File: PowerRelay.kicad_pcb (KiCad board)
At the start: 2 copper layers, 100 x 100 mm, 26 parts, among them J1 Screw_Terminal_01x03, J2 Conn_01x20_Female, J3 Conn_01x20_Female, J4 Conn_01x02_Female, J5 Screw_Terminal_01x03, J6 Screw_Terminal_01x03, J7 Conn_01x02_Female, K1 G5LE-1A4_DC3, K2 G5LE-1A4_DC3, Q1 2N7000, Q2 2N7000

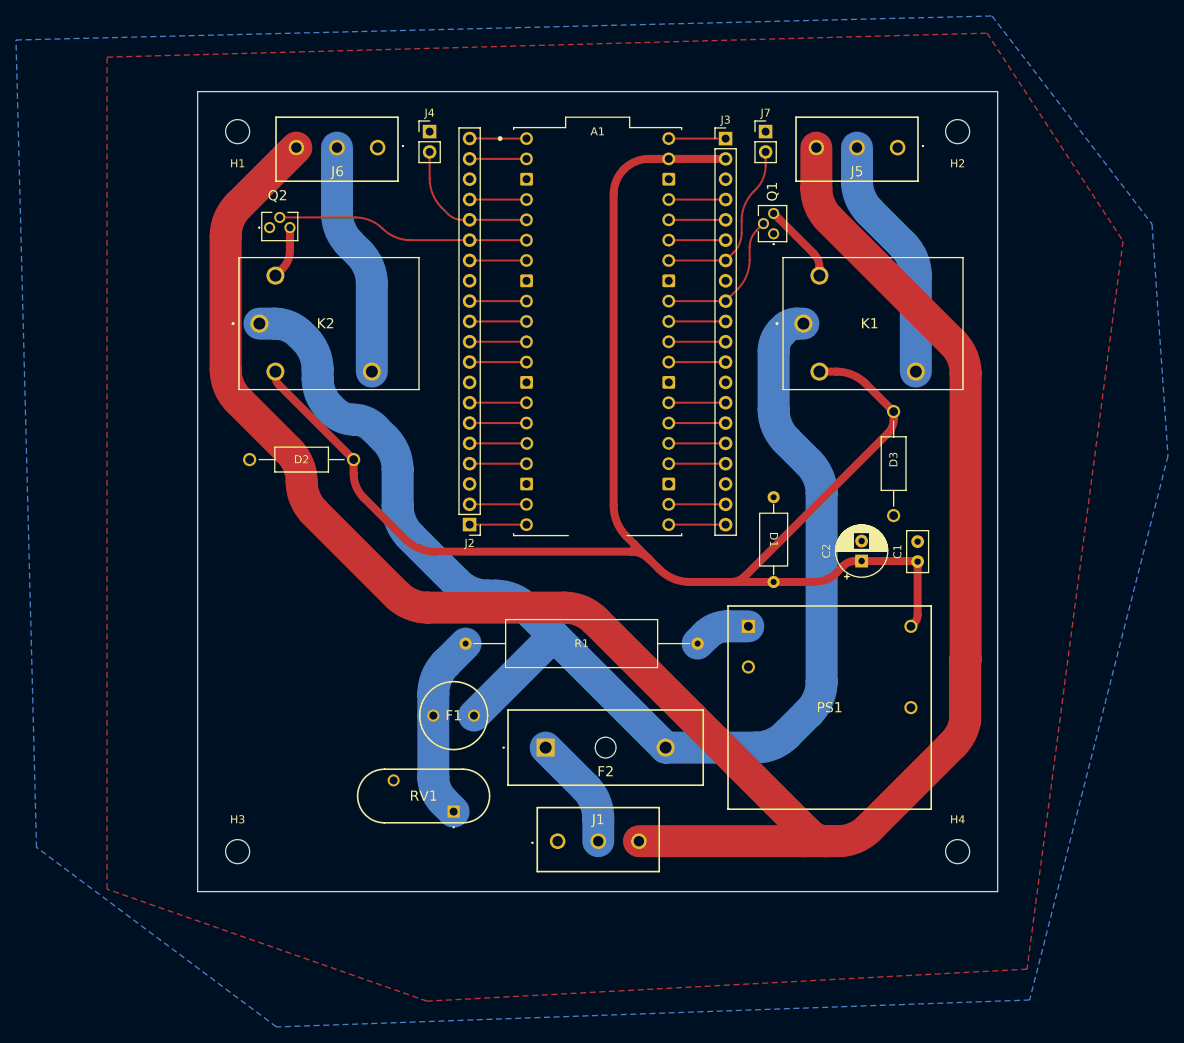
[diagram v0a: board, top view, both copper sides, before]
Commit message: add power label for ac power connectors to silkscreen
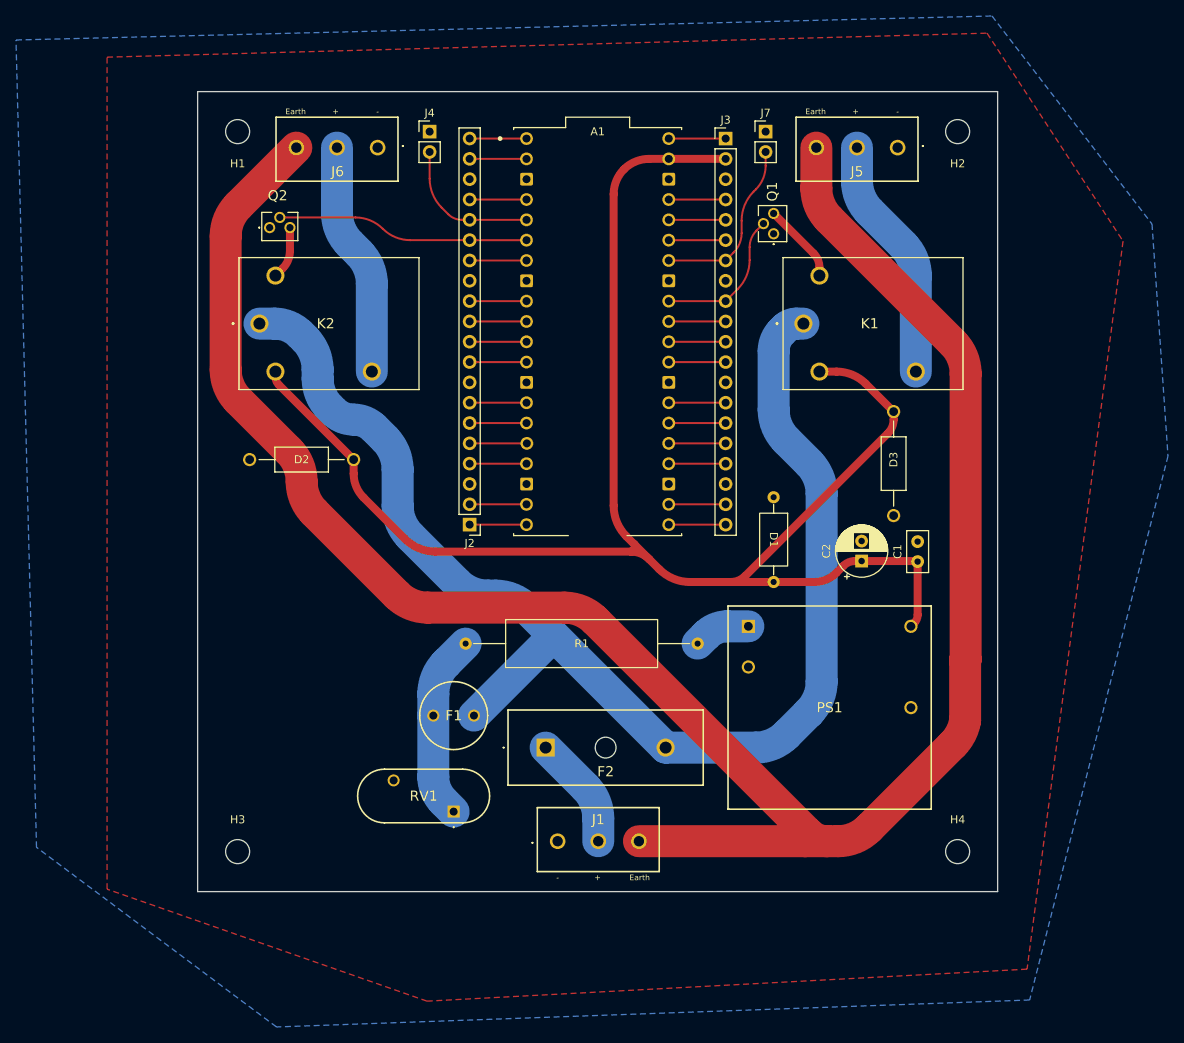
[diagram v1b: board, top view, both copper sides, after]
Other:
- board text added: "+"
- board text added: "-"
- board text added: "Earth"
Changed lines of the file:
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@@
   )
   (gr_rect (start 50 50) (end 150 150) (layer "Edge.Cuts") (width 0.1) (fill none))
+  (gr_text "-" (at 95 148.25) (layer "F.SilkS")
+    (effects (font (size 0.7 0.7) (thickness 0.15)))
+  )
+  (gr_text "+" (at 67.25 52.5) (layer "F.SilkS")
+    (effects (font (size 0.7 0.7) (thickness 0.15)))
+  )
+  (gr_text "-" (at 72.5 52.5) (layer "F.SilkS")
+    (effects (font (size 0.7 0.7) (thickness 0.15)))
+  )
+  (gr_text "Earth" (at 62.25 52.5) (layer "F.SilkS")
+    (effects (font (size 0.7 0.7) (thickness 0.15)))
+  )
+  (gr_text "Earth" (at 127.25 52.5) (layer "F.SilkS")
+    (effects (font (size 0.7 0.7) (thickness 0.15)))
+  )
+  (gr_text "-" (at 137.5 52.5) (layer "F.SilkS")
+    (effects (font (size 0.7 0.7) (thickness 0.15)))
+  )
+  (gr_text "Earth" (at 105.25 148.25) (layer "F.SilkS")
+    (effects (font (size 0.7 0.7) (thickness 0.15)))
+  )
+  (gr_text "+" (at 132.25 52.5) (layer "F.SilkS")
+    (effects (font (size 0.7 0.7) (thickness 0.15)))
+  )
+  (gr_text "+" (at 100 148.25) (layer "F.SilkS")
+    (effects (font (size 0.7 0.7) (thickness 0.15)))
+  )
   (segment (start 59.725 85.6125) (end 59.725 85) (width 1) (layer "F.Cu") (net 1))
   (segment (start 104.546896 106.546896) (end 106.453104 108.453104) (width 1) (layer "F.Cu") (net 1))

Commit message: added intruction for later
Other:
- board text added: "put wire connector here move pico back to accomidate"
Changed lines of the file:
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@@
     (pad "" np_thru_hole circle (at 0 0) (size 3 3) (drill 3) (layers *.Cu *.Mask))
   )
+  (gr_rect (start 96 52) (end 104 55) (layer "Dwgs.User") (width 0.15) (fill none))
   (gr_rect (start 50 50) (end 150 150) (layer "Edge.Cuts") (width 0.1) (fill none))
   (gr_text "-" (at 95 148.25) (layer "F.SilkS")
@@
     (effects (font (size 0.7 0.7) (thickness 0.15)))
   )
+  (gr_text "put wire connector here move pico back to accomidate" (at 100 53) (layer "Dwgs.User")
+    (effects (font (size 1 1) (thickness 0.15)))
+  )
   (segment (start 59.725 85.6125) (end 59.725 85) (width 1) (layer "F.Cu") (net 1))

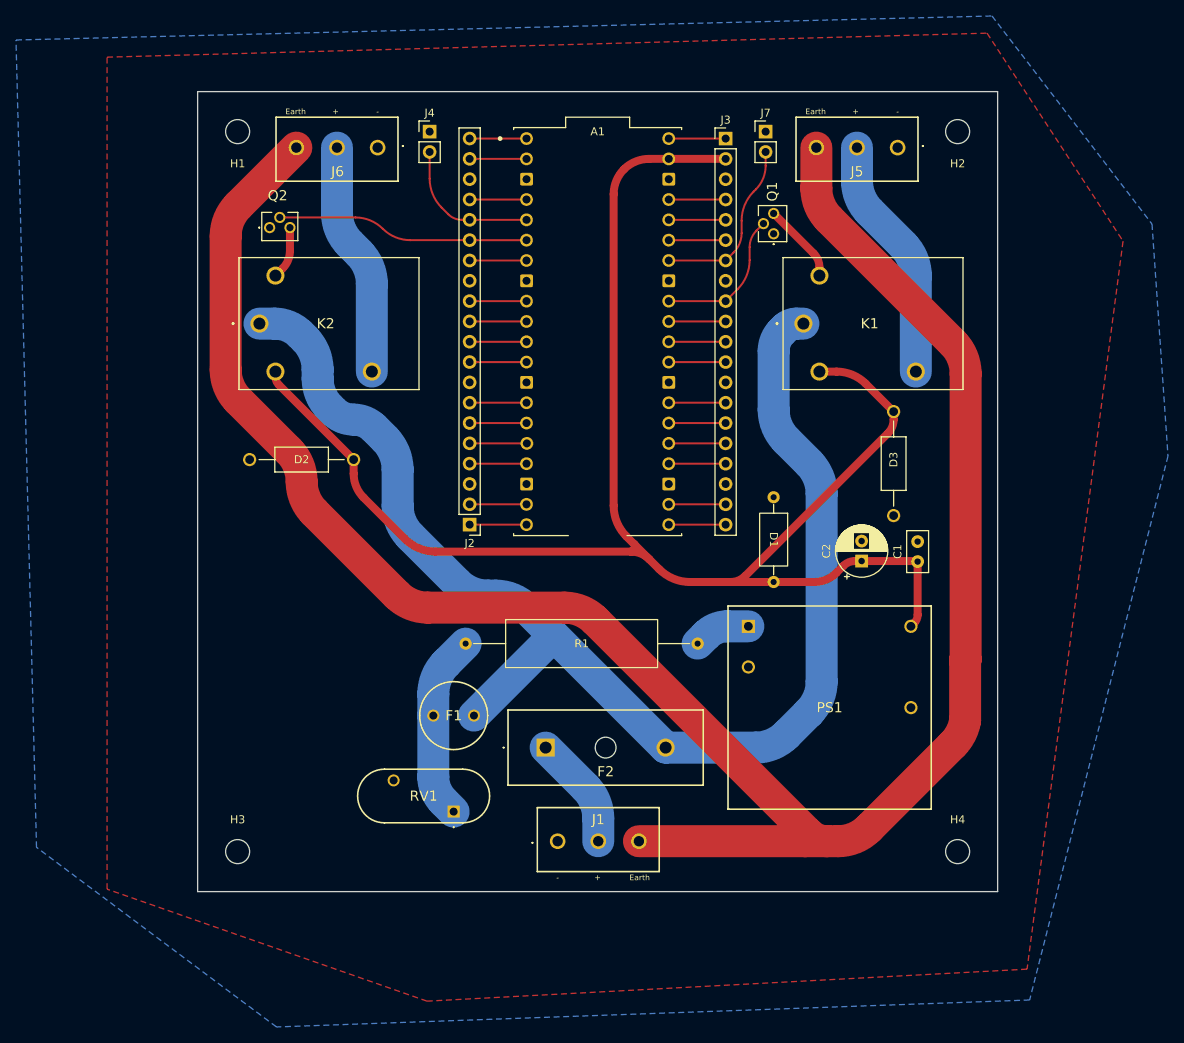
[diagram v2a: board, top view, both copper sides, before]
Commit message: add aux port for inter board comunication
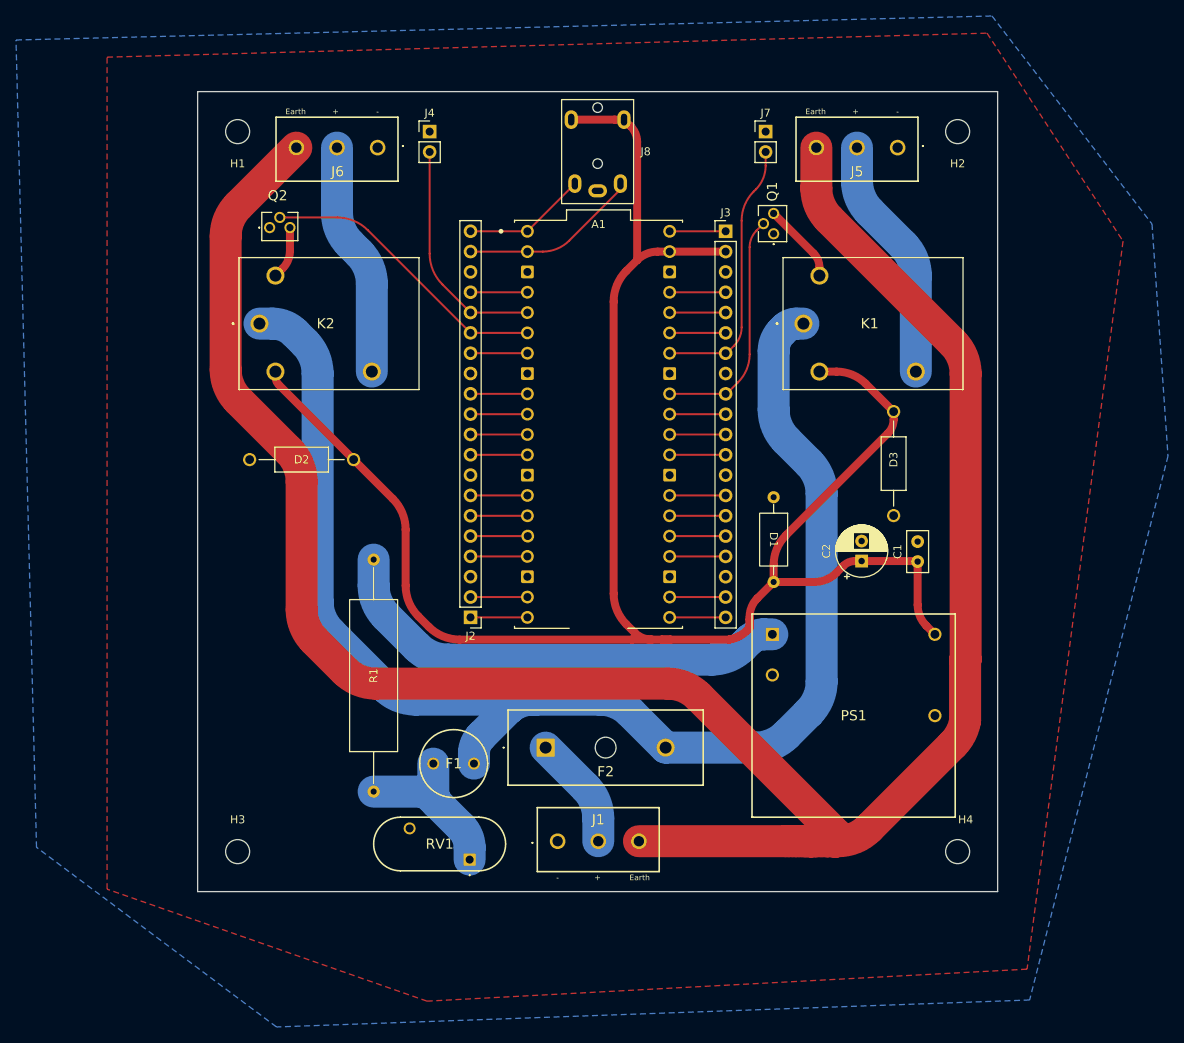
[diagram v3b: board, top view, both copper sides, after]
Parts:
- added J8: AudioJack4, 54-00174:54-00174_JACK, F.Cu at (103.5, 50.0)
- moved R1 26.3 mm to (72.0, 123.0), turned to 90 degrees
- moved A1 11.6 mm to (100.1, 91.6)
- moved J2 11.6 mm to (84.1, 115.7)
- moved J3 11.6 mm to (116.0, 67.5)
- moved RV1 6.32 mm to (84.0, 146.0)
- moved F1 6.00 mm to (84.5, 134.0)
- moved PS1 3.16 mm to (121.8, 117.8)
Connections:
- net Net-(A1-Pad1) renamed TX
- net Net-(A1-Pad2) renamed RX
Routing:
- net Net-(PS1-Pad1): track 7.06 -> 58.6 mm
- net +3V3: track 209.3 -> 246.1 mm
- net RX: track 7.11 -> 22.4 mm
- net Heating: track 18.4 -> 29.9 mm
- net VAC: track 166.3 -> 177.6 mm
- net Cooling Switch: track 18.5 -> 29.0 mm
- net Heating SW: track 23.0 -> 33.5 mm
- net Earth: track 260.7 -> 270.9 mm
- net TX: track 7.11 -> 15.5 mm
- net Cooling: track 31.5 -> 36.7 mm
- net Net-(F1-Pad2): track 23.3 -> 22.7 mm
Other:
- board text removed: "put wire connector here move pico back to accomidate"

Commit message: add logo to board
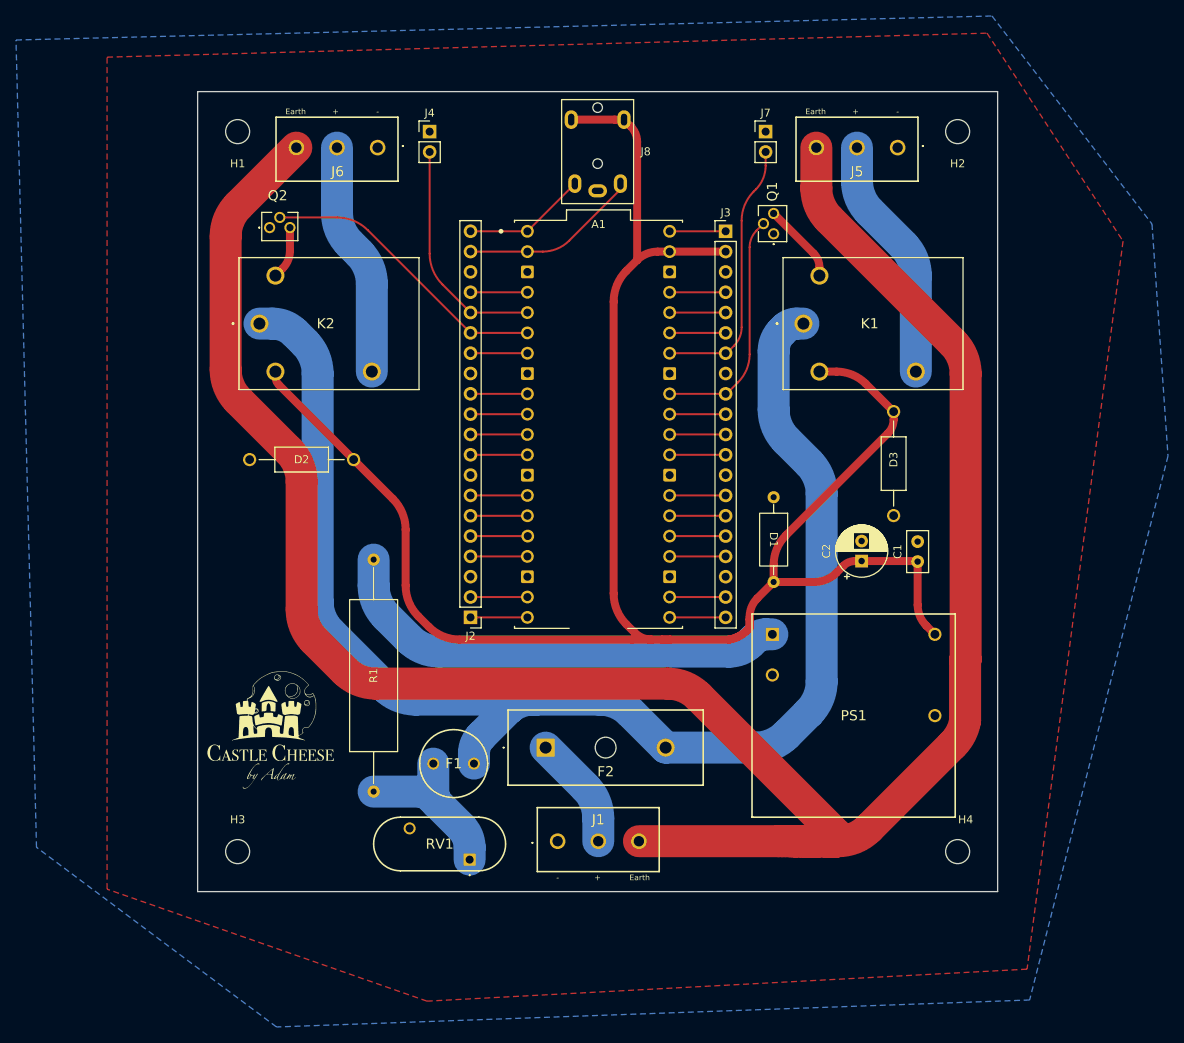
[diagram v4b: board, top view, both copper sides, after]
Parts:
- added G***: LOGO, PCB:Logo, F.Cu at (59.0, 130.0)
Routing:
- net Net-(PS1-Pad1): track 58.6 -> 57.9 mm

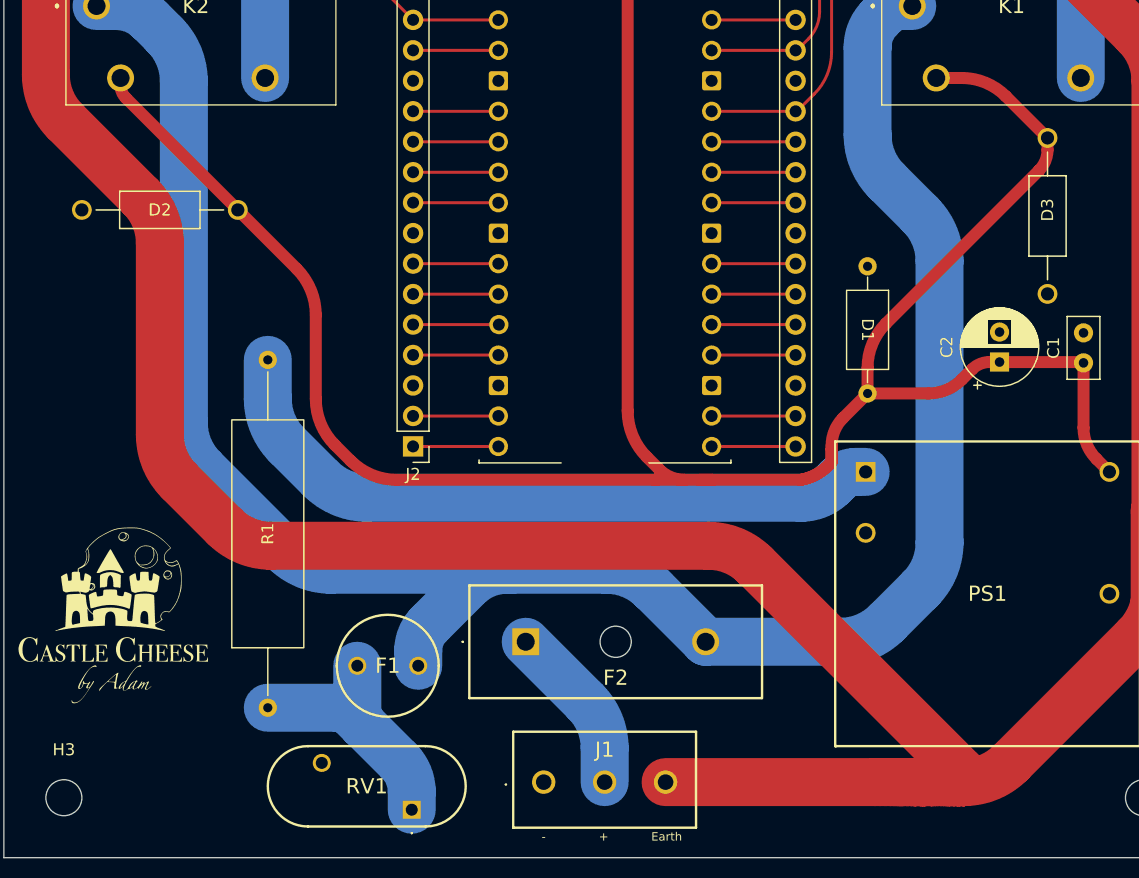
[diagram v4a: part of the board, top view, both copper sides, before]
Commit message: make space to shift power headers back
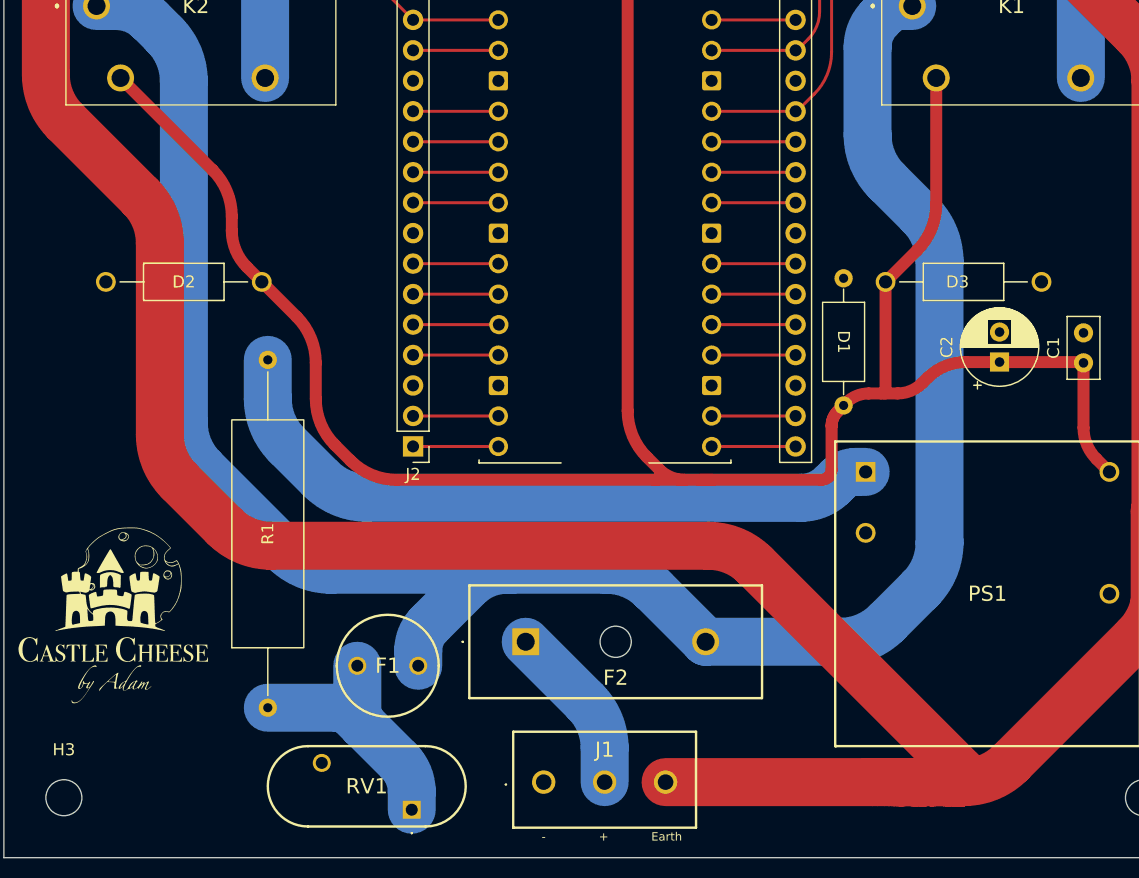
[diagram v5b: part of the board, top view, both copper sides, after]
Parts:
- added G***: LOGO, PCB:Back, B.Cu at (117.1, 122.9)
- moved D3 8.90 mm to (130.0, 102.0), turned to 0 degrees
- moved D2 6.32 mm to (65.0, 102.0)
- moved D1 2.24 mm to (120.0, 107.0)
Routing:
- net +3V3: track 246.1 -> 235.0 mm
